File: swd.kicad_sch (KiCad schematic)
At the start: 1 part, among them J5 Conn_02x03_Odd_Even

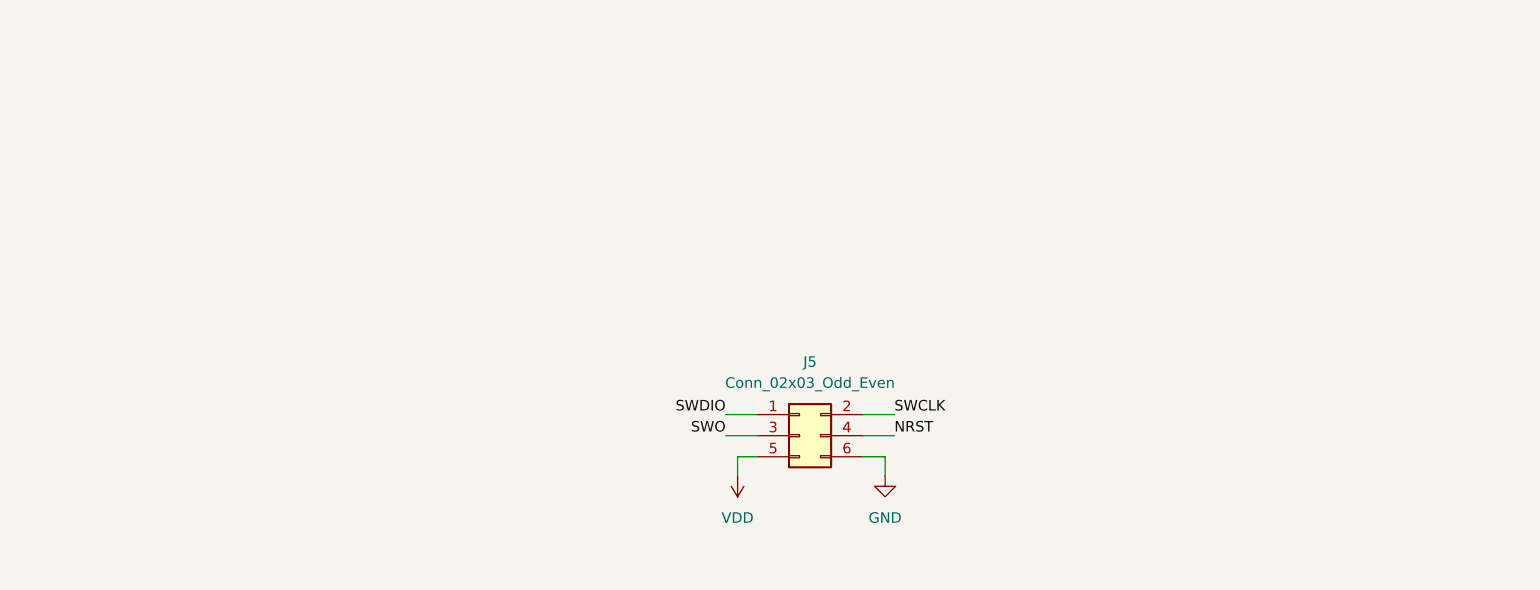
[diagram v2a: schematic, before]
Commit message: Fixed GPS, Radio, Baro, STM32, and added/rearanged some sheets (#26)
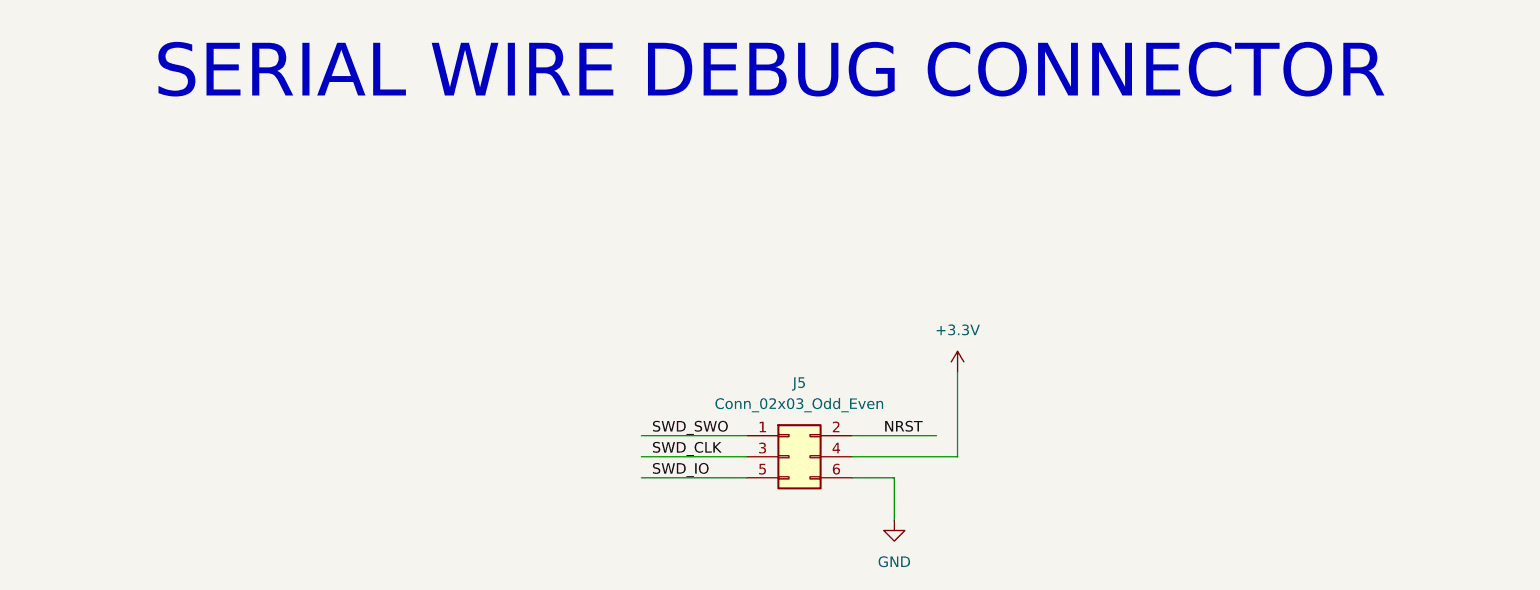
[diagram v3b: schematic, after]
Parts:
- J5: footprint Connector_PinHeader_1.27mm:PinHeader_2x03_P1.27mm_Vertical -> (none)
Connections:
- net SWCLK is gone; now on net NRST: J5.2 (Pin_2)
- net NRST: no longer J5.4 (Pin_4)
- net SWDIO renamed SWD_SWO
- net SWO renamed SWD_CLK
- net VDD renamed SWD_IO
- new net +3.3V: J5.4 (Pin_4)
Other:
- note added: "SERIAL WIRE DEBUG CONNECTOR"
